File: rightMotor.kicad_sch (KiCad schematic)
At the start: 0 parts

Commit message: updated motor driver files
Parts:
- added U3: ~, symbol sumo-robot-symbols:TB6612FNG
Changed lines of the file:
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@@
 	(generator_version "9.0")
 	(paper "A4")
+	(symbol
+		(lib_id "sumo-robot-symbols:TB6612FNG")
+		(at 129.54 111.76 0)
+		(unit 1)
+		(exclude_from_sim no)
+		(in_bom yes)
+		(on_board yes)
+		(dnp no)
+		(property "Reference" "U3"
+			(at 130.556 77.216 0)
+			(effects
+				(font
+					(size 1.27 1.27)
+				)
+			)
+		)
+		(property "Value" "~"
+			(at 146.685 74.93 0)
+			(effects
+				(font
+					(size 1.27 1.27)
+				)
+			)
+		)
+		(property "Footprint" ""
+			(at 129.54 111.76 0)
+			(effects
+				(font
+					(size 1.27 1.27)
+				)
+				(hide yes)
+			)
+		)
+		(property "Datasheet" ""
+			(at 129.54 111.76 0)
+			(effects
+				(font
+					(size 1.27 1.27)
+				)
+				(hide yes)
+			)
+		)
+		(property "Description" ""
+			(at 129.54 111.76 0)
+			(effects
+				(font
+					(size 1.27 1.27)
+				)
+				(hide yes)
+			)
+		)
+		(pin "8"
+		)
+		(pin "23"
+		)
+		(pin "13"
+		)
+		(pin "16"
+		)
+		(pin "9"
+		)
+		(pin "6"
+		)
+		(pin "5"
+		)
+		(pin "10"
+		)
+		(pin "1"
+		)
+		(pin "24"
+		)
+		(pin "21"
+		)
+		(pin "19"
+		)
+		(pin "22"
+		)
+		(pin "2"
+		)
+		(pin "18"
+		)
+		(pin "15"
+		)
+		(pin "4"
+		)
+		(pin "3"
+		)
+		(pin "17"
+		)
+		(pin "14"
+		)
+		(pin "11"
+		)
+		(pin "7"
+		)
+		(pin "12"
+		)
+		(pin "20"
+		)
+		(instances
+			(project ""
+				(path "/f283bc71-7763-4093-b75c-cbe2f5868c12/f1956493-43e6-4247-bc8c-3efab023d950"
+					(reference "U3")
+					(unit 1)
+				)
+			)
+		)
+	)
 )

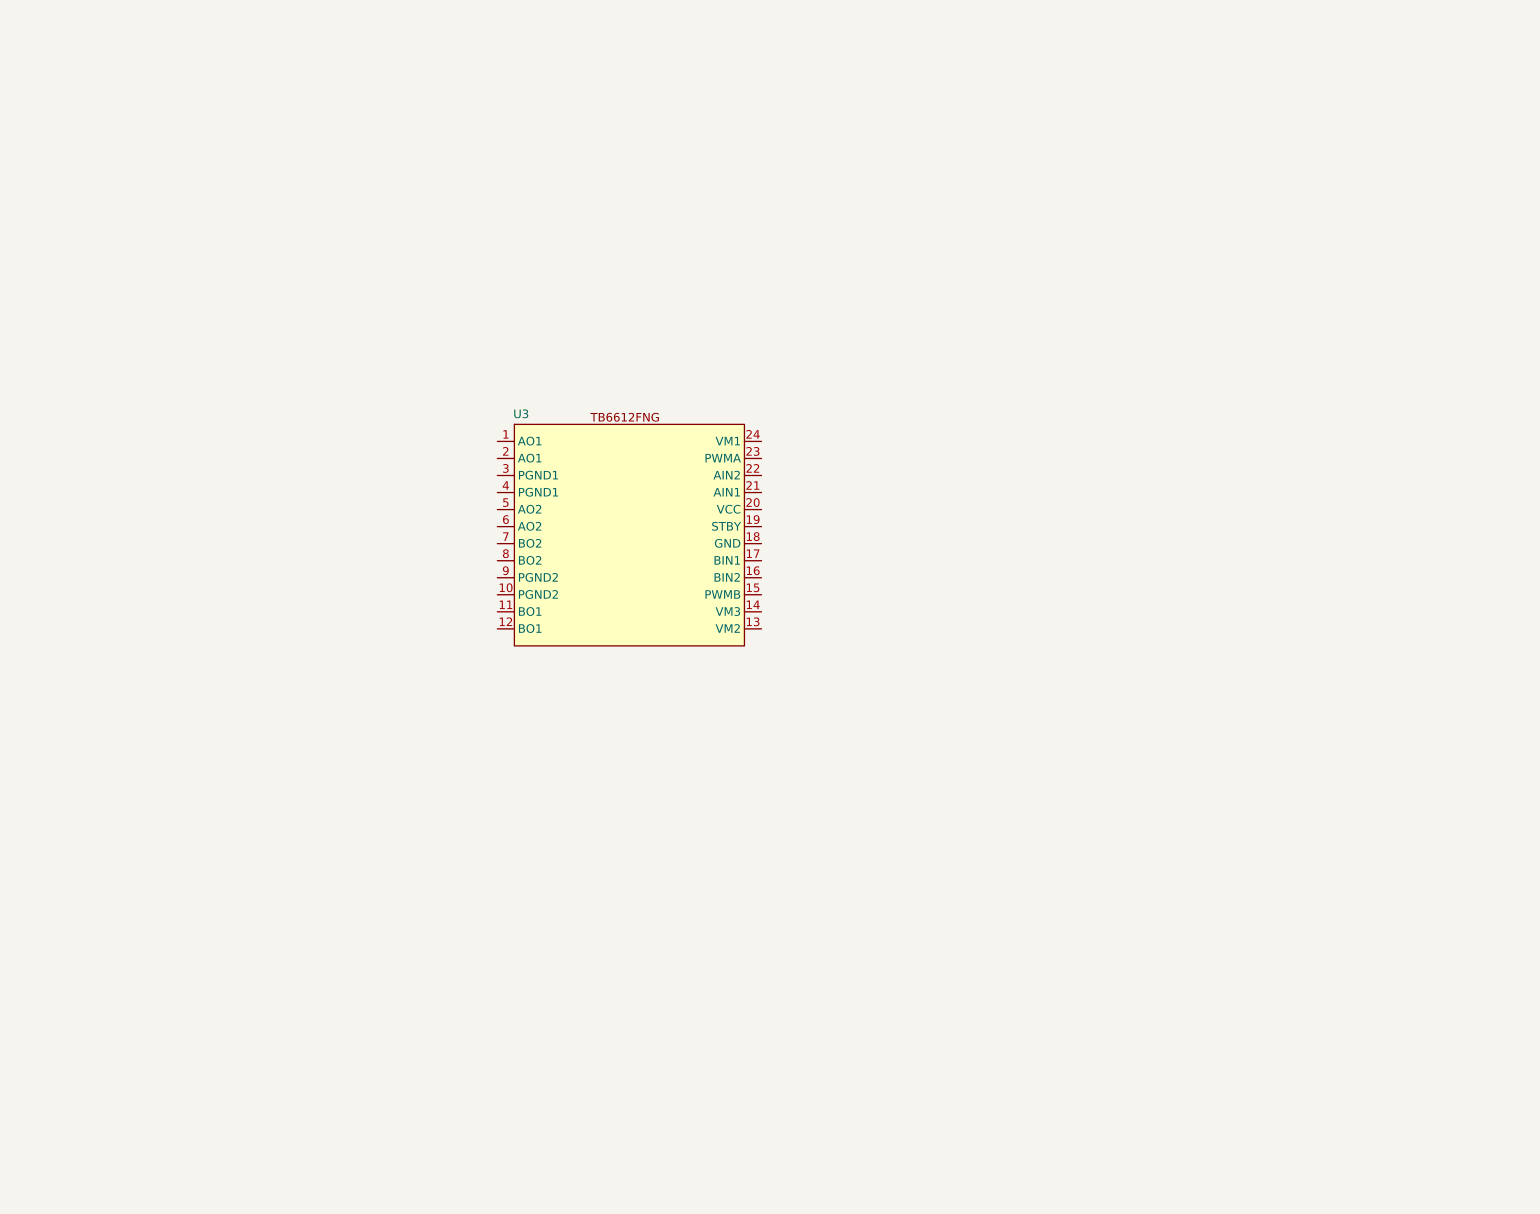
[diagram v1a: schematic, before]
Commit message: started adding DC Motor controller logic
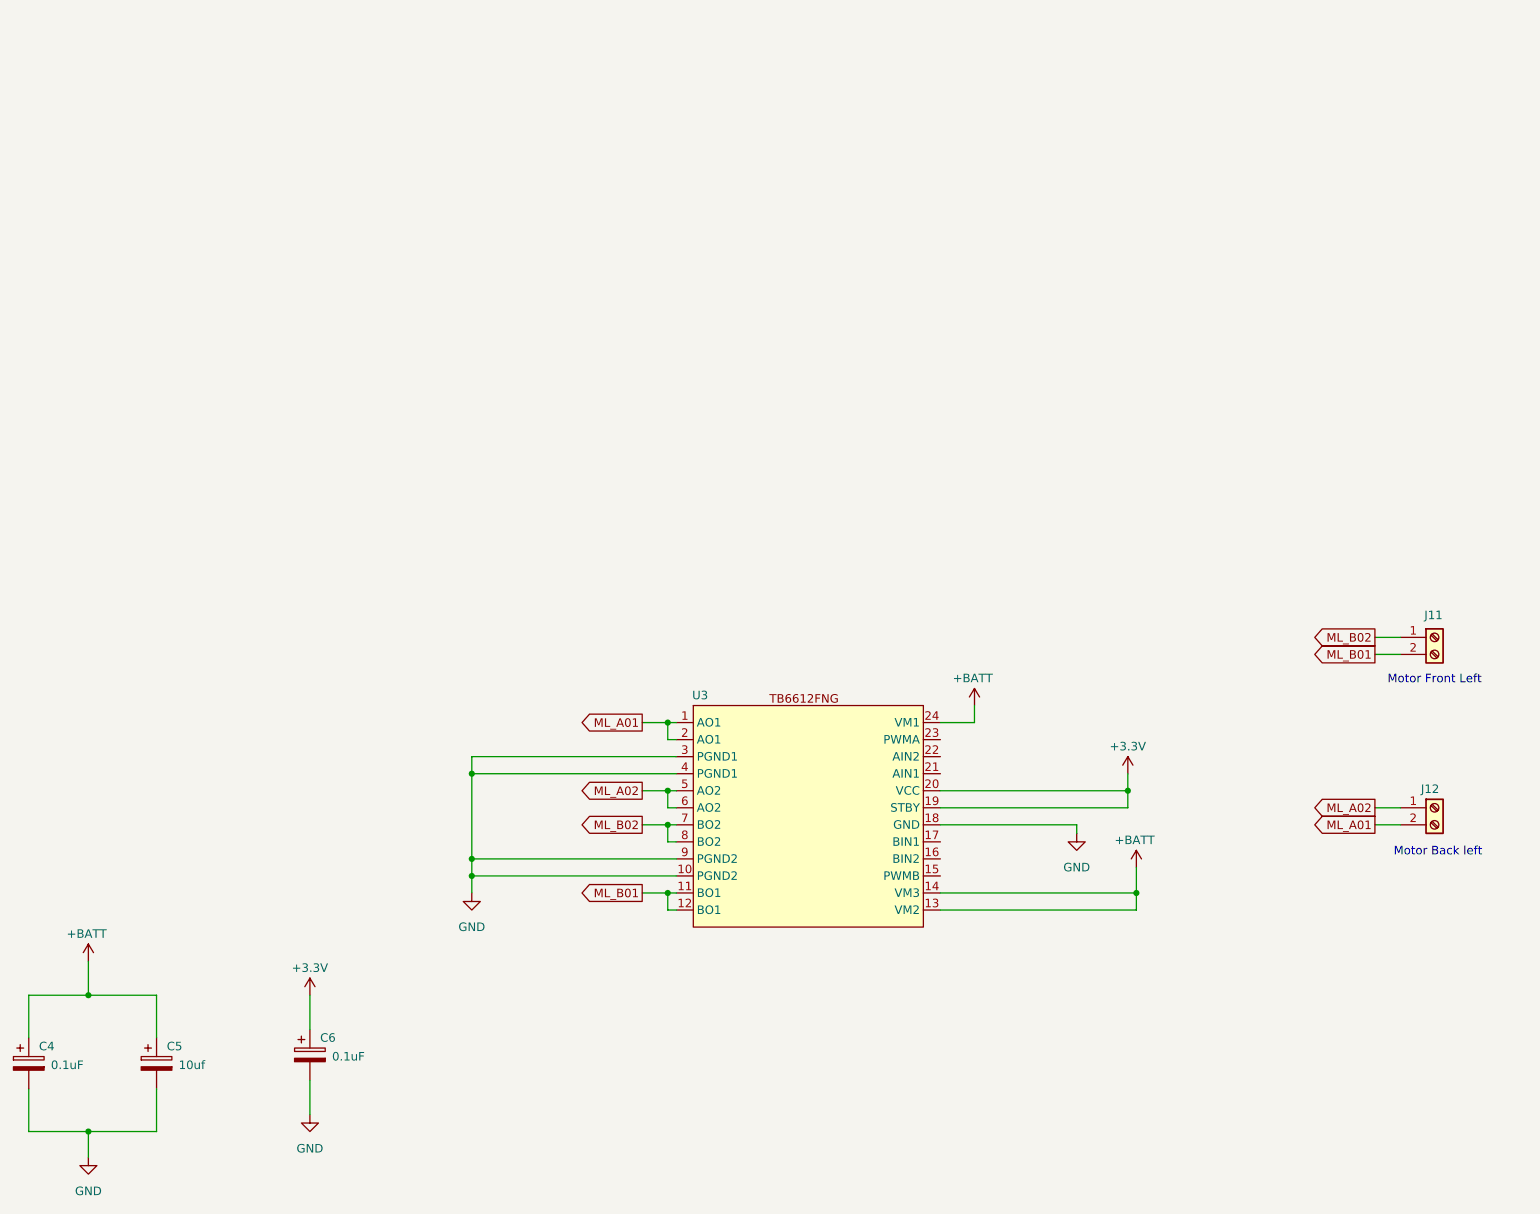
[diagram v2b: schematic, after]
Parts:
- added C4, C6: 0.1uF, symbol Device:C_Polarized
- added C5: 10uf, symbol Device:C_Polarized
- added J11: ~, symbol Connector:Screw_Terminal_01x02
- added J12: Screw_Terminal_01x02, symbol Connector:Screw_Terminal_01x02
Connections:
- net ML_A01: now reaches U3.1 (AO1)
- net ML_A01: now also U3.2 (AO1), J12.2 (Pin_2)
- net GND: now reaches U3.10 (PGND2)
- net GND: now also U3.18 (GND), U3.3 (PGND1), U3.4 (PGND1), U3.9 (PGND2), C4.2, C5.2, C6.2
- net ML_B01: now reaches U3.11 (BO1)
- net ML_B01: now also U3.12 (BO1), J11.2 (Pin_2)
- net +BATT: now reaches U3.13 (VM2)
- net +BATT: now also U3.14 (VM3), U3.24 (VM1), C4.1, C5.1
- net +3.3V: now reaches U3.19 (STBY)
- net +3.3V: now also U3.20 (VCC), C6.1
- net ML_A02: now reaches U3.5 (AO2)
- net ML_A02: now also U3.6 (AO2), J12.1 (Pin_1)
- net ML_B02: now reaches U3.7 (BO2)
- net ML_B02: now also U3.8 (BO2), J11.1 (Pin_1)
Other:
- note added: "Motor Back left"
- note added: "Motor Front Left"
- moved on the sheet: U3

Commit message: added motor functionality to the MCU
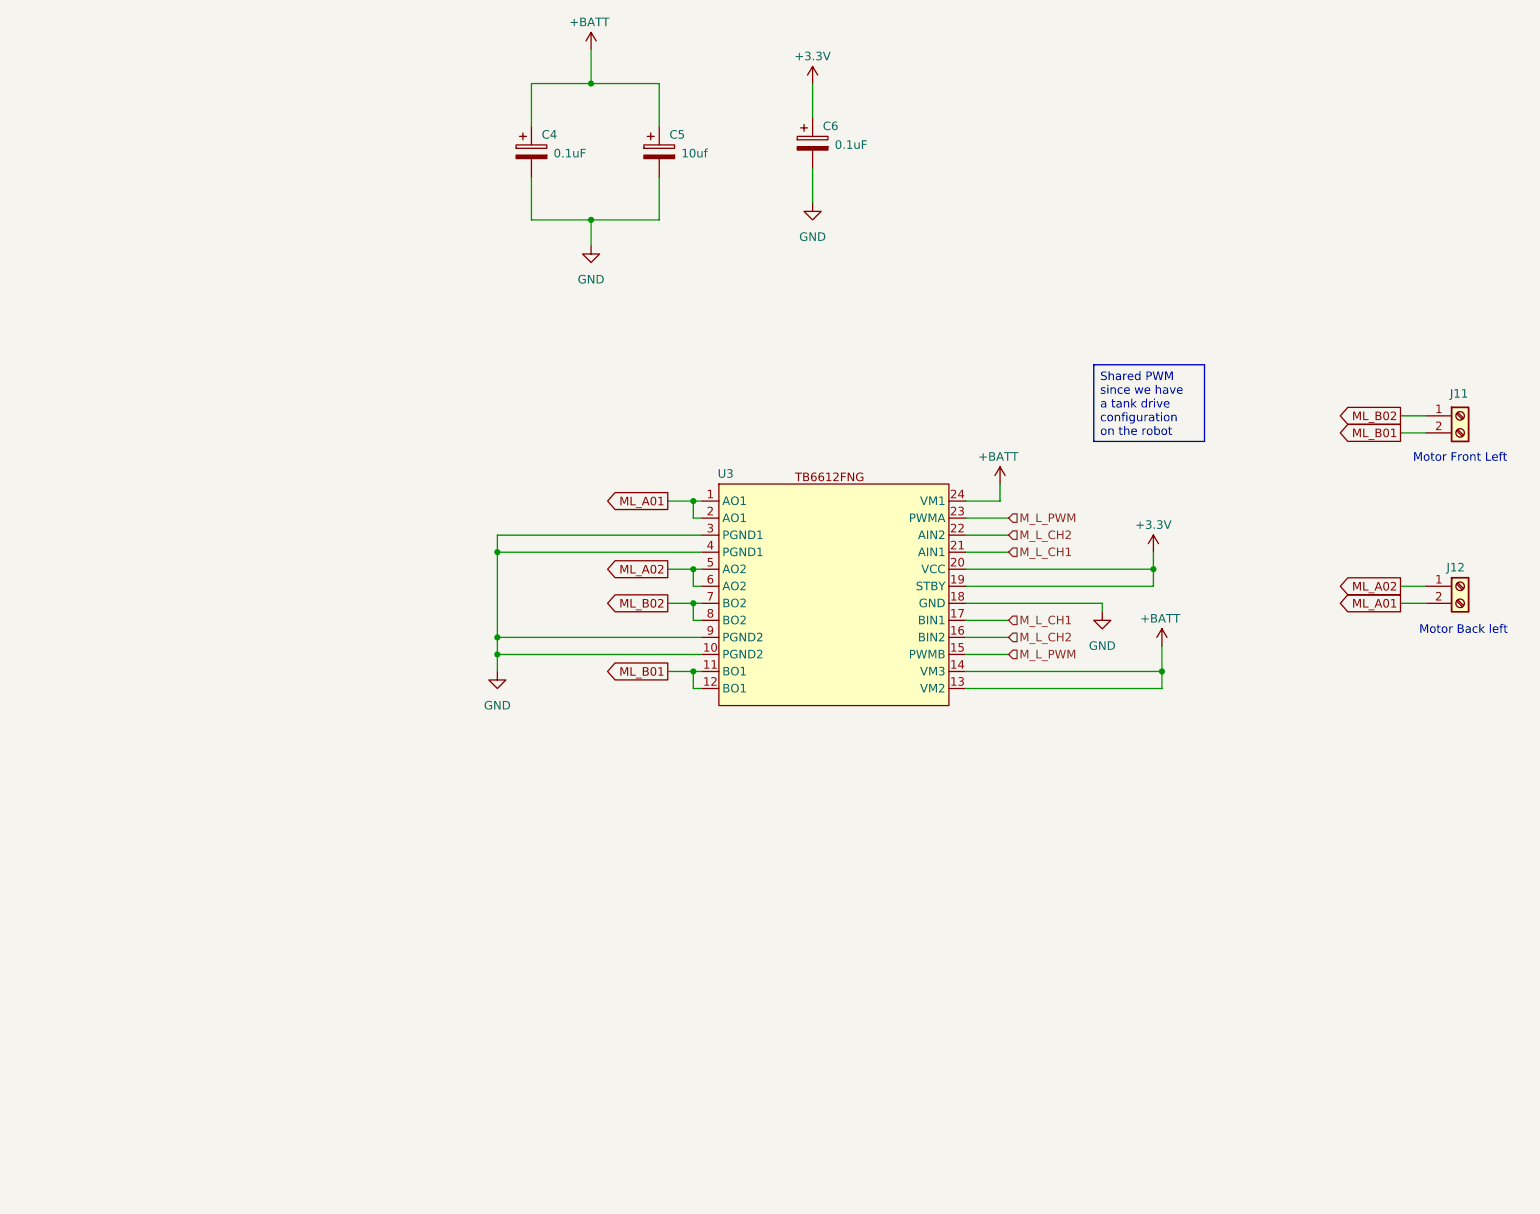
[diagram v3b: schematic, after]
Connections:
- net M_L_PWM: now reaches U3.15 (PWMB)
- net M_L_PWM: now also U3.23 (PWMA)
- net M_L_CH2: now reaches U3.16 (BIN2)
- net M_L_CH2: now also U3.22 (AIN2)
- net M_L_CH1: now reaches U3.17 (BIN1)
- net M_L_CH1: now also U3.21 (AIN1)
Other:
- moved on the sheet: C4, C5, C6, J11, J12, U3

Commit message: added all footprints and step files to components
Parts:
- C4, C5, C6: footprint (none) -> Capacitor_SMD:C_1210_3225Metric
- J11, J12: footprint (none) -> TerminalBlock_Phoenix:TerminalBlock_Phoenix_MKDS-1,5-2_1x02_P5.00mm_Horizontal
- U3: footprint (none) -> Package_SO:SSOP-24_5.3x8.2mm_P0.65mm
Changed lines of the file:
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@@
 			)
 		)
-		(property "Footprint" ""
+		(property "Footprint" "Capacitor_SMD:C_1210_3225Metric"
 			(at 152.0952 41.91 0)
 			(effects
@@
 			)
 		)
-		(property "Footprint" ""
+		(property "Footprint" "Capacitor_SMD:C_1210_3225Metric"
 			(at 133.0452 41.91 0)
 			(effects
@@
 			)
 		)
-		(property "Footprint" ""
+		(property "Footprint" "TerminalBlock_Phoenix:TerminalBlock_Phoenix_MKDS-1,5-2_1x02_P5.00mm_Horizontal"
 			(at 270.51 102.87 0)
 			(effects
@@
 			)
 		)
-		(property "Footprint" ""
+		(property "Footprint" "Package_SO:SSOP-24_5.3x8.2mm_P0.65mm"
 			(at 160.02 120.65 0)
 			(effects
@@
 			)
 		)
-		(property "Footprint" ""
+		(property "Footprint" "TerminalBlock_Phoenix:TerminalBlock_Phoenix_MKDS-1,5-2_1x02_P5.00mm_Horizontal"
 			(at 270.51 77.47 0)
 			(effects
@@
 			)
 		)
-		(property "Footprint" ""
+		(property "Footprint" "Capacitor_SMD:C_1210_3225Metric"
 			(at 174.9552 40.64 0)
 			(effects

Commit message: updated infomration on schematic; started working on layout
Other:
- company: (none) -> Erick Zamora 
- title: (none) -> Miniature Sumo Robot 
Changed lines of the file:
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@@
 	(generator_version "9.0")
 	(paper "A4")
+	(title_block
+		(title "Miniature Sumo Robot ")
+		(date "2025-09-26")
+		(rev "A")
+		(company "Erick Zamora ")
+	)
 	(text "Motor Back left "
 		(exclude_from_sim no)

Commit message: Updated PCB Layers and Schematics
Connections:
- net GND: no longer U3.10 (PGND2), U3.4 (PGND1)
- net ML_A01: no longer U3.2 (AO1)
- net ML_A02: no longer U3.6 (AO2)
- net ML_B01: no longer U3.12 (BO1)
- net ML_B02: no longer U3.8 (BO2)
- no-connect marks 0 -> 6
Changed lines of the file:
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@@
-	)
-	(junction
-		(at 156.21 105.41)
-		(diameter 0)
-		(color 0 0 0 0)
-	)
-	(junction
-		(at 156.21 90.17)
-		(diameter 0)
-		(color 0 0 0 0)
 	)
 	(junction
@@
 	)
 	(junction
-		(at 127 97.79)
-		(diameter 0)
-		(color 0 0 0 0)
-	)
-	(junction
-		(at 127 113.03)
-		(diameter 0)
-		(color 0 0 0 0)
-	)
-	(junction
 		(at 224.79 100.33)
 		(diameter 0)
@@
 	)
 	(junction
-		(at 156.21 115.57)
-		(diameter 0)
-		(color 0 0 0 0)
-	)
-	(junction
 		(at 127 110.49)
 		(diameter 0)
@@
 		(color 0 0 0 0)
 	)
-	(junction
-		(at 156.21 100.33)
-		(diameter 0)
-		(color 0 0 0 0)
+	(no_connect
+		(at 157.48 113.03)
+	)
+	(no_connect
+		(at 157.48 118.11)
+	)
+	(no_connect
+		(at 157.48 92.71)
+	)
+	(no_connect
+		(at 157.48 107.95)
+	)
+	(no_connect
+		(at 157.48 97.79)
+	)
+	(no_connect
+		(at 157.48 102.87)
 	)
 	(wire
@@
 	(wire
 		(pts
-			(xy 127 113.03) (xy 157.48 113.03)
-		)
-		(stroke
-			(width 0)
-			(type default)
-		)
-	)
-	(wire
-		(pts
 			(xy 196.85 113.03) (xy 203.2 113.03)
 		)
@@
 	(wire
 		(pts
-			(xy 152.4 115.57) (xy 156.21 115.57)
-		)
-		(stroke
-			(width 0)
-			(type default)
-		)
-	)
-	(wire
-		(pts
 			(xy 196.85 95.25) (xy 203.2 95.25)
 		)
@@
 	(wire
 		(pts
-			(xy 152.4 100.33) (xy 156.21 100.33)
-		)
-		(stroke
-			(width 0)
-			(type default)
-		)
-	)
-	(wire
-		(pts
 			(xy 140.97 48.26) (xy 140.97 52.07)
 		)
@@
 	(wire
 		(pts
-			(xy 156.21 118.11) (xy 156.21 115.57)
-		)
-		(stroke
-			(width 0)
-			(type default)
-		)
-	)
-	(wire
-		(pts
-			(xy 157.48 92.71) (xy 156.21 92.71)
-		)
-		(stroke
-			(width 0)
-			(type default)
-		)
-	)
-	(wire
-		(pts
 			(xy 196.85 100.33) (xy 224.79 100.33)
 		)
@@
 	(wire
 		(pts
-			(xy 157.48 102.87) (xy 156.21 102.87)
-		)
-		(stroke
-			(width 0)
-			(type default)
-		)
-	)
-	(wire
-		(pts
 			(xy 127 110.49) (xy 157.48 110.49)
 		)
@@
 	(wire
 		(pts
-			(xy 127 115.57) (xy 127 113.03)
+			(xy 127 110.49) (xy 127 115.57)
 		)
 		(stroke
@@
 	(wire
 		(pts
-			(xy 156.21 105.41) (xy 157.48 105.41)
-		)
-		(stroke
-			(width 0)
-			(type default)
-		)
-	)
-	(wire
-		(pts
-			(xy 156.21 100.33) (xy 157.48 100.33)
+			(xy 152.4 105.41) (xy 157.48 105.41)
+		)
+		(stroke
+			(width 0)
+			(type default)
+		)
+	)
+	(wire
+		(pts
+			(xy 152.4 100.33) (xy 157.48 100.33)
 		)
 		(stroke
@@
 	(wire
 		(pts
-			(xy 156.21 92.71) (xy 156.21 90.17)
-		)
-		(stroke
-			(width 0)
-			(type default)
-		)
-	)
-	(wire
-		(pts
-			(xy 156.21 107.95) (xy 156.21 105.41)
-		)
-		(stroke
-			(width 0)
-			(type default)
-		)
-	)
-	(wire
-		(pts
 			(xy 261.62 105.41) (xy 265.43 105.41)
 		)
@@
 	(wire
 		(pts
-			(xy 127 113.03) (xy 127 110.49)
-		)
-		(stroke
-			(width 0)
-			(type default)
-		)
-	)
-	(wire
-		(pts
 			(xy 196.85 107.95) (xy 203.2 107.95)
 		)
@@
 	(wire
 		(pts
-			(xy 152.4 90.17) (xy 156.21 90.17)
-		)
-		(stroke
-			(width 0)
-			(type default)
-		)
-	)
-	(wire
-		(pts
-			(xy 157.48 118.11) (xy 156.21 118.11)
-		)
-		(stroke
-			(width 0)
-			(type default)
-		)
-	)
-	(wire
-		(pts
-			(xy 152.4 105.41) (xy 156.21 105.41)
-		)
-		(stroke
-			(width 0)
-			(type default)
-		)
-	)
-	(wire
-		(pts
 			(xy 201.93 90.17) (xy 201.93 87.63)
 		)
@@
 	(wire
 		(pts
-			(xy 156.21 90.17) (xy 157.48 90.17)
-		)
-		(stroke
-			(width 0)
-			(type default)
-		)
-	)
-	(wire
-		(pts
-			(xy 157.48 107.95) (xy 156.21 107.95)
-		)
-		(stroke
-			(width 0)
-			(type default)
-		)
-	)
-	(wire
-		(pts
-			(xy 156.21 115.57) (xy 157.48 115.57)
+			(xy 152.4 90.17) (xy 157.48 90.17)
+		)
+		(stroke
+			(width 0)
+			(type default)
+		)
+	)
+	(wire
+		(pts
+			(xy 152.4 115.57) (xy 157.48 115.57)
 		)
 		(stroke
@@
 	(wire
 		(pts
-			(xy 127 97.79) (xy 157.48 97.79)
-		)
-		(stroke
-			(width 0)
-			(type default)
-		)
-	)
-	(wire
-		(pts
-			(xy 156.21 102.87) (xy 156.21 100.33)
-		)
-		(stroke
-			(width 0)
-			(type default)
-		)
-	)
-	(wire
-		(pts
 			(xy 173.99 27.94) (xy 173.99 33.02)
 		)
@@
 	(wire
 		(pts
-			(xy 127 110.49) (xy 127 97.79)
-		)
-		(stroke
-			(width 0)
-			(type default)
-		)
-	)
-	(wire
-		(pts
 			(xy 132.08 41.91) (xy 132.08 48.26)
 		)
@@
 	(wire
 		(pts
-			(xy 127 95.25) (xy 127 97.79)
-		)
-		(stroke
+			(xy 127 95.25) (xy 127 110.49)
+		)
+		(stroke
